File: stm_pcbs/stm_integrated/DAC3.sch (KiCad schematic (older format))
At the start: 21 parts, among them P3 BNC, U7 AD8676, U8 AD5791, U9 AD8675

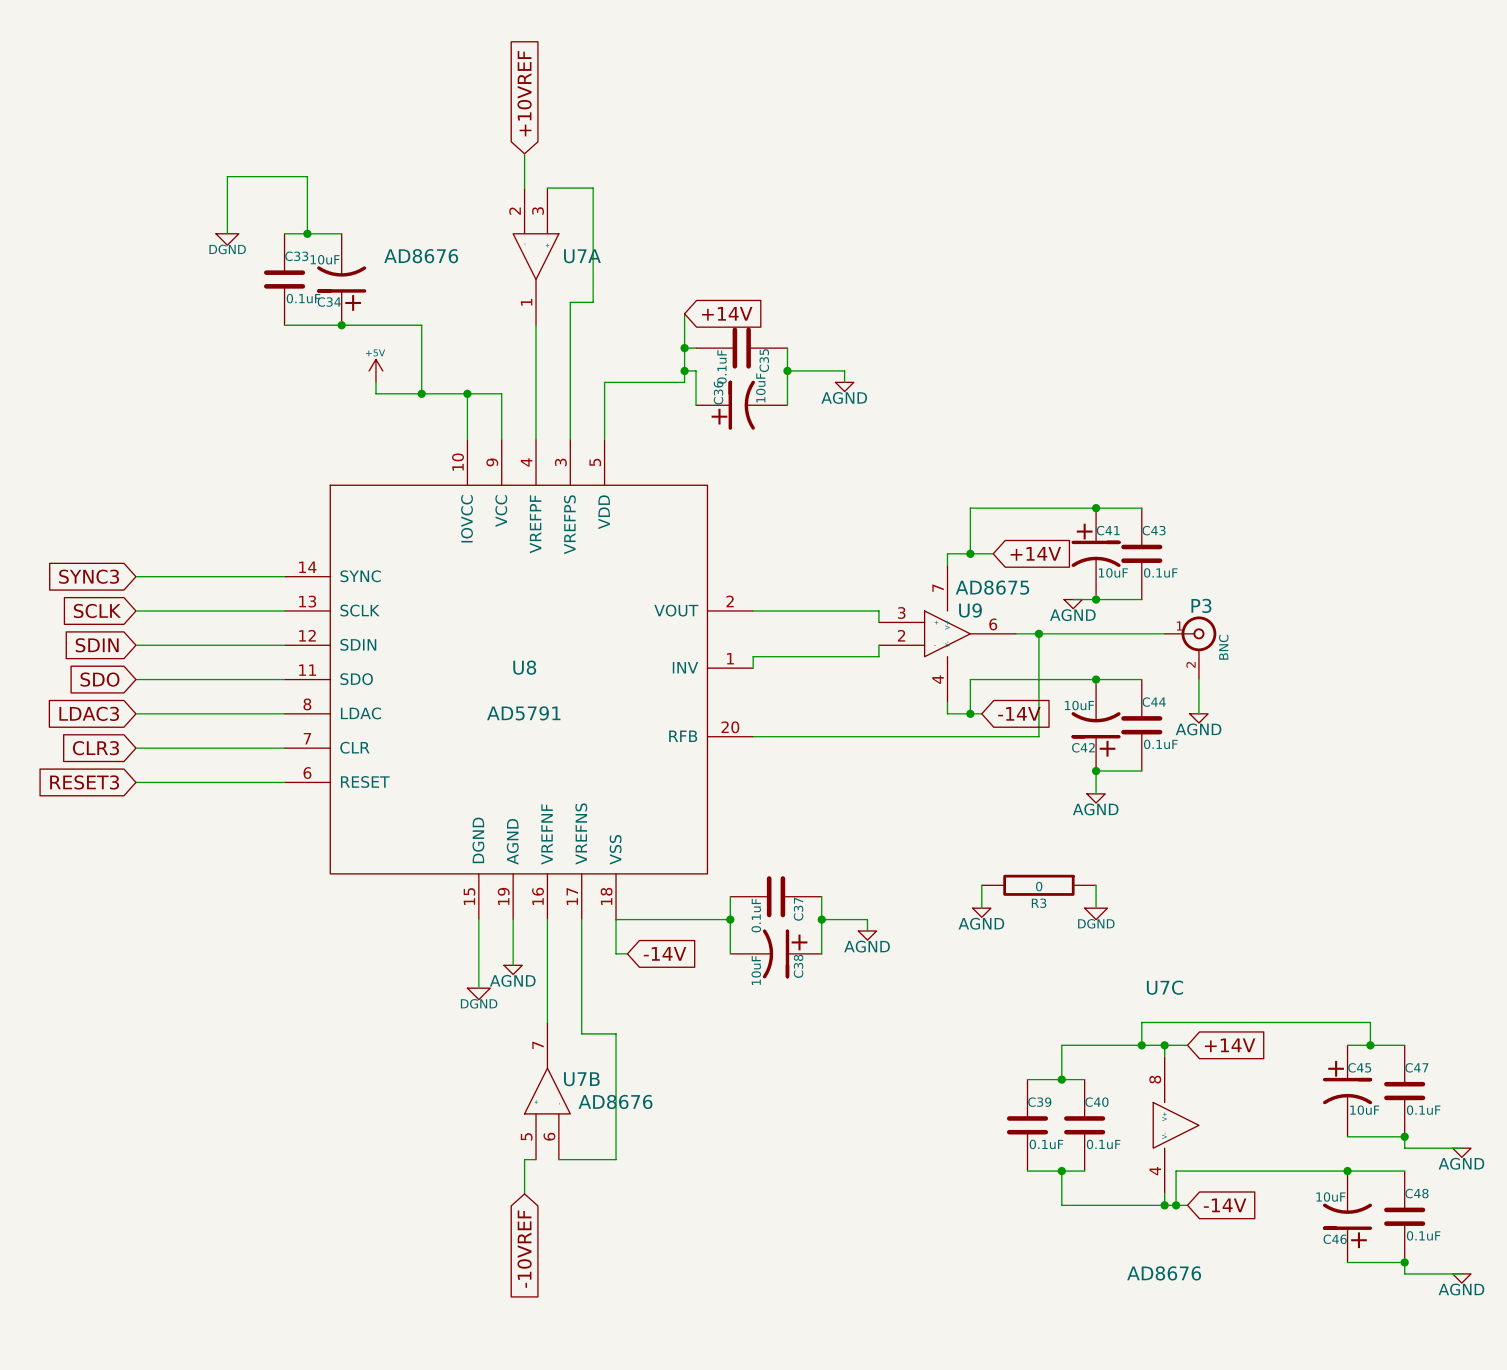
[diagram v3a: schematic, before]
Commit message: fixed issue with DAC (opamp wiring was wrong)
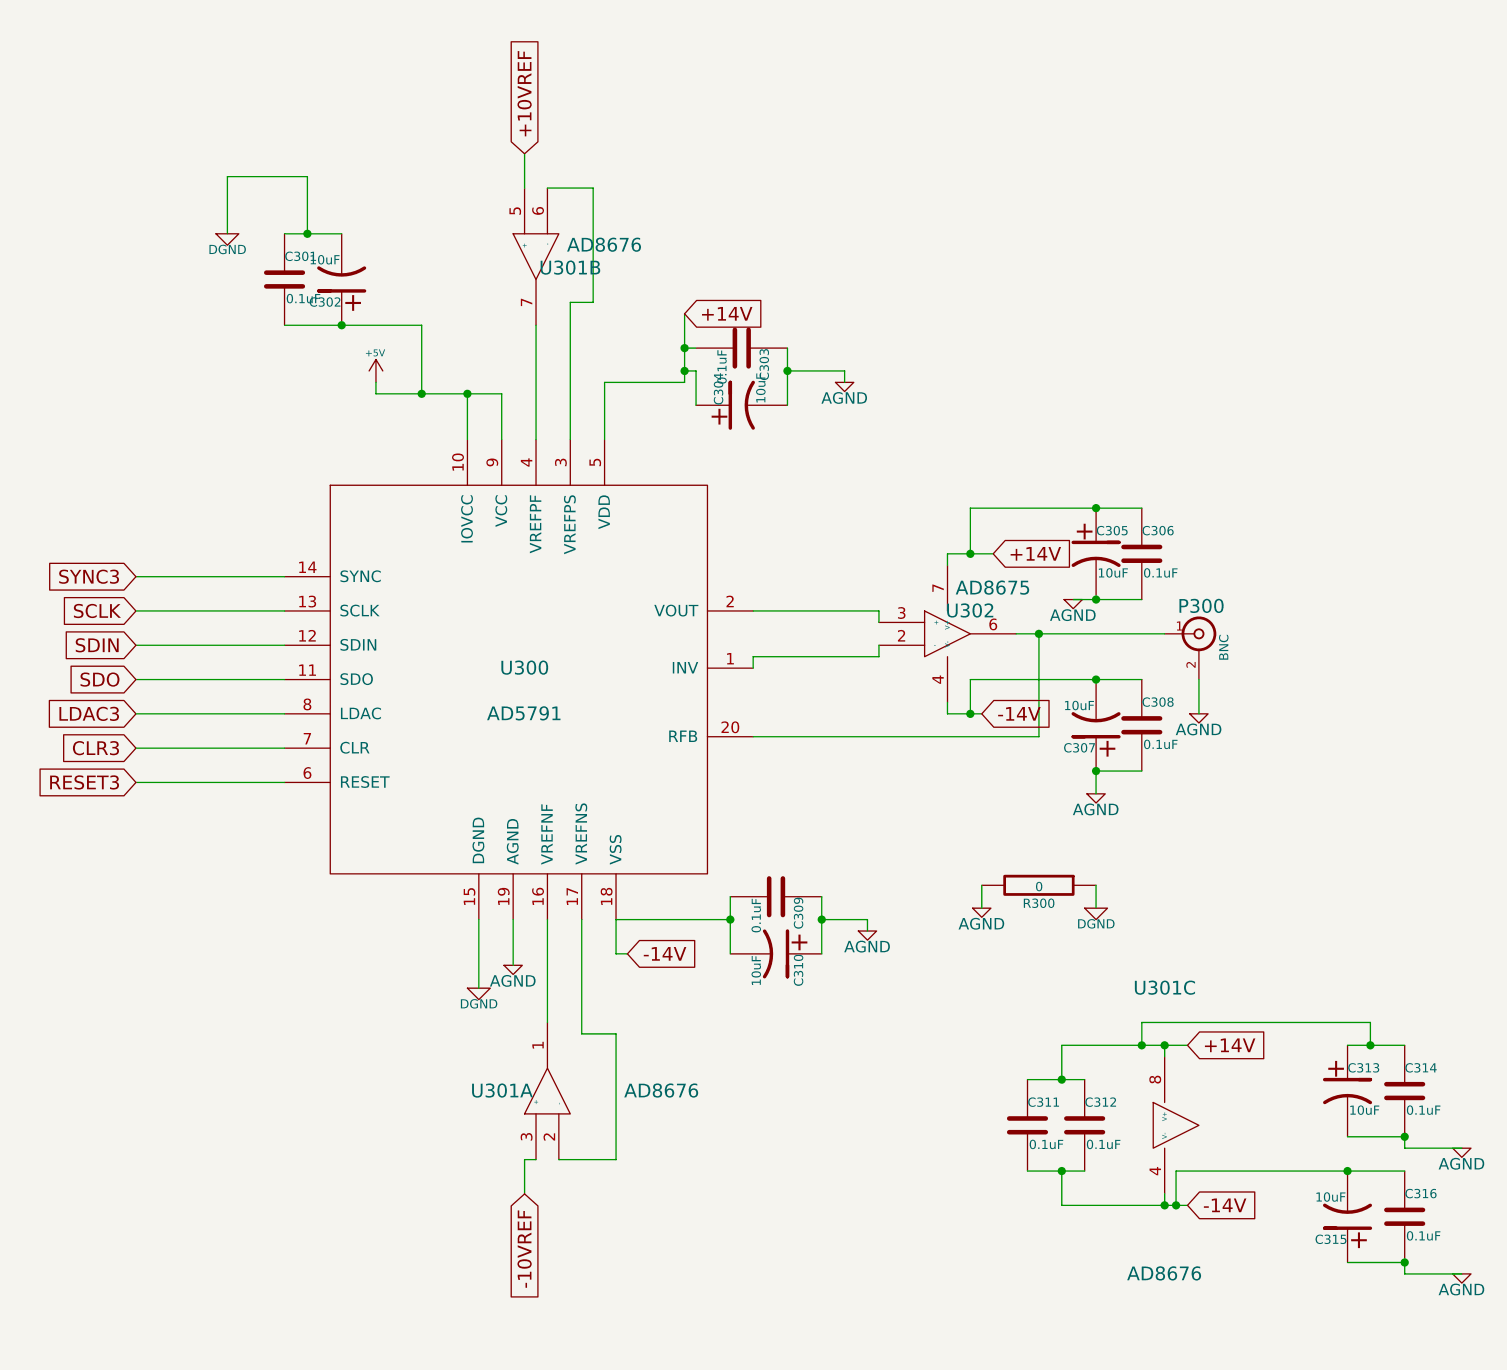
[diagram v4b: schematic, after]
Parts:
- renumbered C33 to C301, C34 to C302, C35 to C303, C36 to C304, C41 to C305, C43 to C306, C42 to C307, C44 to C308, C37 to C309, C38 to C310, C39 to C311, C40 to C312, C45 to C313, C47 to C314, C46 to C315, C48 to C316, P3 to P300, R3 to R300, U8 to U300, U7 to U301, U9 to U302
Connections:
- net +10VREF: now also U301.5 (+); no longer U301.2 (-)
- net -10VREF: now also U301.3 (+); no longer U301.5 (+)
- net at U300.16 (VREFNF): now also U301.1; no longer U301.7
- net at U300.17 (VREFNS): now also U301.2 (-); no longer U301.6 (-)
- net at U300.3 (VREFPS): now also U301.6 (-); no longer U301.3 (+)
- net at U300.4 (VREFPF): now also U301.7; no longer U301.1
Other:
- moved on the sheet: U301A, U301B
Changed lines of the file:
@@
 $EndDescr
 $Comp
-L ad5791:AD5791 U8
+L ad5791:AD5791 U300
 U 1 1 5A25F8A7
 P 5150 3800
-F 0 "U8" H 5000 4000 60  0000 C CNN
+F 0 "U300" H 5000 4000 60  0000 C CNN
 F 1 "AD5791" H 5000 3800 60  0000 C CNN
 F 2 "stm:SSOP-20" H 5150 3850 60  0001 C CNN
@@
 $EndComp
 $Comp
-L ad5791:AD8675 U9
+L ad5791:AD8675 U302
 U 1 1 5A25F8AE
 P 6850 3450
-F 0 "U9" H 6950 3550 60  0000 C CNN
+F 0 "U302" H 6950 3550 60  0000 C CNN
 F 1 "AD8675" H 7050 3650 60  0000 C CNN
 F 2 "stm:SOIC-8" H 7050 3400 60  0001 C CNN
@@
 $EndComp
 $Comp
-L ad5791:AD8676 U7
+L ad5791:AD8676 U301
 U 1 1 5A25F8B5
+P 5100 5500
+F 0 "U301" V 5150 5700 60  0000 C CNN
+F 1 "AD8676" V 5150 5000 60  0000 C CNN
+F 2 "stm:SOIC-8" H 5250 5500 60  0001 C CNN
+F 3 "" H 5250 5500 60  0000 C CNN
+	1    5100 5500
+	0    -1   -1   0
+$EndComp
+$Comp
+L ad5791:AD8676 U301
+U 2 1 5A25F8BC
 P 5050 1750
-F 0 "U7" V 5100 1950 60  0000 C CNN
-F 1 "AD8676" V 5100 1250 60  0000 C CNN
+F 0 "U301" V 5150 1600 60  0000 C CNN
+F 1 "AD8676" V 5050 1450 60  0000 C CNN
 F 2 "stm:SOIC-8" H 5200 1750 60  0001 C CNN
 F 3 "" H 5200 1750 60  0000 C CNN
-	1    5050 1750
-	0    1    1    0
-$EndComp
-$Comp
-L ad5791:AD8676 U7
-U 2 1 5A25F8BC
-P 5100 5500
-F 0 "U7" V 5200 5350 60  0000 C CNN
-F 1 "AD8676" V 5100 5200 60  0000 C CNN
-F 2 "stm:SOIC-8" H 5250 5500 60  0001 C CNN
-F 3 "" H 5250 5500 60  0000 C CNN
-	2    5100 5500
-	0    -1   -1   0
-$EndComp
-$Comp
-L ad5791:AD8676 U7
+	2    5050 1750
+	0    -1   1    0
+$EndComp
+$Comp
+L ad5791:AD8676 U301
 U 3 1 5A25F8C3
 P 7800 5600
-F 0 "U7" H 7800 6200 60  0000 C CNN
+F 0 "U301" H 7800 6200 60  0000 C CNN
 F 1 "AD8676" H 7800 4950 60  0000 C CNN
 F 2 "stm:SOIC-8" H 7950 5600 60  0001 C CNN
@@
 $EndComp
 $Comp
-L device:BNC P3
+L device:BNC P300
 U 1 1 5A25F8CA
 P 7950 3450
-F 0 "P3" H 7960 3570 60  0000 C CNN
+F 0 "P300" H 7960 3570 60  0000 C CNN
 F 1 "BNC" V 8060 3390 40  0000 C CNN
 F 2 "stm:SMA" H 7950 3450 60  0001 C CNN
@@
 $EndComp
 $Comp
-L device:C C35
+L device:C C303
 U 1 1 5A25F8EC
 P 5950 2200
-F 0 "C35" H 5950 2300 40  0000 L CNN
+F 0 "C303" H 5950 2300 40  0000 L CNN
 F 1 "0.1uF" H 5956 2115 40  0000 L CNN
 F 2 "Capacitors_SMD:C_0805_HandSoldering" H 5988 2050 30  0001 C CNN
@@
 $EndComp
 $Comp
-L device:C C37
+L device:C C309
 U 1 1 5A25F8F9
 P 6100 4600
-F 0 "C37" H 6100 4700 40  0000 L CNN
+F 0 "C309" H 6100 4700 40  0000 L CNN
 F 1 "0.1uF" H 6106 4515 40  0000 L CNN
 F 2 "Capacitors_SMD:C_0805_HandSoldering" H 6138 4450 30  0001 C CNN
@@
 $EndComp
 $Comp
-L device:C C33
+L device:C C301
 U 1 1 5A25F914
 P 3950 1900
-F 0 "C33" H 3950 2000 40  0000 L CNN
+F 0 "C301" H 3950 2000 40  0000 L CNN
 F 1 "0.1uF" H 3956 1815 40  0000 L CNN
 F 2 "Capacitors_SMD:C_0805_HandSoldering" H 3988 1750 30  0001 C CNN
@@
 $EndComp
 $Comp
-L device:C C40
+L device:C C312
 U 1 1 5A25F921
 P 7450 5600
-F 0 "C40" H 7450 5700 40  0000 L CNN
+F 0 "C312" H 7450 5700 40  0000 L CNN
 F 1 "0.1uF" H 7456 5515 40  0000 L CNN
 F 2 "Capacitors_SMD:C_0805_HandSoldering" H 7488 5450 30  0001 C CNN
@@
 $EndComp
 $Comp
-L device:C C47
+L device:C C314
 U 1 1 5A25F928
 P 8850 5450
-F 0 "C47" H 8850 5550 40  0000 L CNN
+F 0 "C314" H 8850 5550 40  0000 L CNN
 F 1 "0.1uF" H 8856 5365 40  0000 L CNN
 F 2 "Capacitors_SMD:C_0805_HandSoldering" H 8888 5300 30  0001 C CNN
@@
 $EndComp
 $Comp
-L device:C C48
+L device:C C316
 U 1 1 5A25F92F
 P 8850 6000
-F 0 "C48" H 8850 6100 40  0000 L CNN
+F 0 "C316" H 8850 6100 40  0000 L CNN
 F 1 "0.1uF" H 8856 5915 40  0000 L CNN
 F 2 "Capacitors_SMD:C_0805_HandSoldering" H 8888 5850 30  0001 C CNN
@@
 $EndComp
 $Comp
-L device:C C39
+L device:C C311
 U 1 1 5A25F942
 P 7200 5600
-F 0 "C39" H 7200 5700 40  0000 L CNN
+F 0 "C311" H 7200 5700 40  0000 L CNN
 F 1 "0.1uF" H 7206 5515 40  0000 L CNN
 F 2 "Capacitors_SMD:C_0805_HandSoldering" H 7238 5450 30  0001 C CNN
@@
 $EndComp
 $Comp
-L device:CP1 C45
+L device:CP1 C313
 U 1 1 5A25F949
 P 8600 5450
-F 0 "C45" H 8600 5550 40  0000 L CNN
+F 0 "C313" H 8600 5550 40  0000 L CNN
 F 1 "10uF" H 8606 5365 40  0000 L CNN
 F 2 "stm:SMD-1210_Pol" H 8638 5300 30  0001 C CNN
@@
 $EndComp
 $Comp
-L device:CP1 C46
+L device:CP1 C315
 U 1 1 5A25F950
 P 8600 6000
-F 0 "C46" H 8600 6100 40  0000 L CNN
+F 0 "C315" H 8600 6100 40  0000 L CNN
 F 1 "10uF" H 8606 5915 40  0000 L CNN
 F 2 "stm:SMD-1210_Pol" H 8638 5850 30  0001 C CNN
@@
 $EndComp
 $Comp
-L device:CP1 C38
+L device:CP1 C310
 U 1 1 5A25F957
 P 6100 4850
-F 0 "C38" H 6100 4950 40  0000 L CNN
+F 0 "C310" H 6100 4950 40  0000 L CNN
 F 1 "10uF" H 6106 4765 40  0000 L CNN
 F 2 "stm:SMD-1210_Pol" H 6138 4700 30  0001 C CNN
@@
 $EndComp
 $Comp
-L device:CP1 C36
+L device:CP1 C304
 U 1 1 5A25F95E
 P 5950 2450
-F 0 "C36" H 5950 2550 40  0000 L CNN
+F 0 "C304" H 5950 2550 40  0000 L CNN
 F 1 "10uF" H 5956 2365 40  0000 L CNN
 F 2 "stm:SMD-1210_Pol" H 5988 2300 30  0001 C CNN
@@
 $EndComp
 $Comp
-L device:CP1 C34
+L device:CP1 C302
 U 1 1 5A25F965
 P 4200 1900
-F 0 "C34" H 4200 2000 40  0000 L CNN
+F 0 "C302" H 4200 2000 40  0000 L CNN
 F 1 "10uF" H 4206 1815 40  0000 L CNN
 F 2 "stm:SMD-1210_Pol" H 4238 1750 30  0001 C CNN
@@
 RESET3
 $Comp
-L device:CP1 C41
+L device:CP1 C305
 U 1 1 5A25F973
 P 7500 3100
-F 0 "C41" H 7500 3200 40  0000 L CNN
+F 0 "C305" H 7500 3200 40  0000 L CNN
 F 1 "10uF" H 7506 3015 40  0000 L CNN
 F 2 "stm:SMD-1210_Pol" H 7538 2950 30  0001 C CNN
@@
 $EndComp
 $Comp
-L device:CP1 C42
+L device:CP1 C307
 U 1 1 5A25F97A
 P 7500 3850
-F 0 "C42" H 7500 3950 40  0000 L CNN
+F 0 "C307" H 7500 3950 40  0000 L CNN
 F 1 "10uF" H 7506 3765 40  0000 L CNN
 F 2 "stm:SMD-1210_Pol" H 7538 3700 30  0001 C CNN
@@
 $EndComp
 $Comp
-L device:C C43
+L device:C C306
 U 1 1 5A25F981
 P 7700 3100
-F 0 "C43" H 7700 3200 40  0000 L CNN
+F 0 "C306" H 7700 3200 40  0000 L CNN
 F 1 "0.1uF" H 7706 3015 40  0000 L CNN
 F 2 "Capacitors_SMD:C_0805_HandSoldering" H 7738 2950 30  0001 C CNN
@@
 $EndComp
 $Comp
-L device:C C44
+L device:C C308
 U 1 1 5A25F988
 P 7700 3850
-F 0 "C44" H 7700 3950 40  0000 L CNN
+F 0 "C308" H 7700 3950 40  0000 L CNN
 F 1 "0.1uF" H 7706 3765 40  0000 L CNN
 F 2 "Capacitors_SMD:C_0805_HandSoldering" H 7738 3700 30  0001 C CNN
@@
 Connection ~ 6950 3800
 $Comp
-L device:R R3
+L device:R R300
 U 1 1 5A25FA0F
 P 7250 4550
-F 0 "R3" V 7330 4550 40  0000 C CNN
+F 0 "R300" V 7330 4550 40  0000 C CNN
 F 1 "0" V 7257 4551 40  0000 C CNN
 F 2 "stm:0Ohm" V 7180 4550 30  0001 C CNN
